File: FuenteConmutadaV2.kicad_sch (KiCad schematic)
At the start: 23 parts, among them J1 Conn_01x01_Pin, J2 Conn_01x01_Pin, J4 Conn_01x01_Pin, J5 USB_C_Receptacle_USB2.0

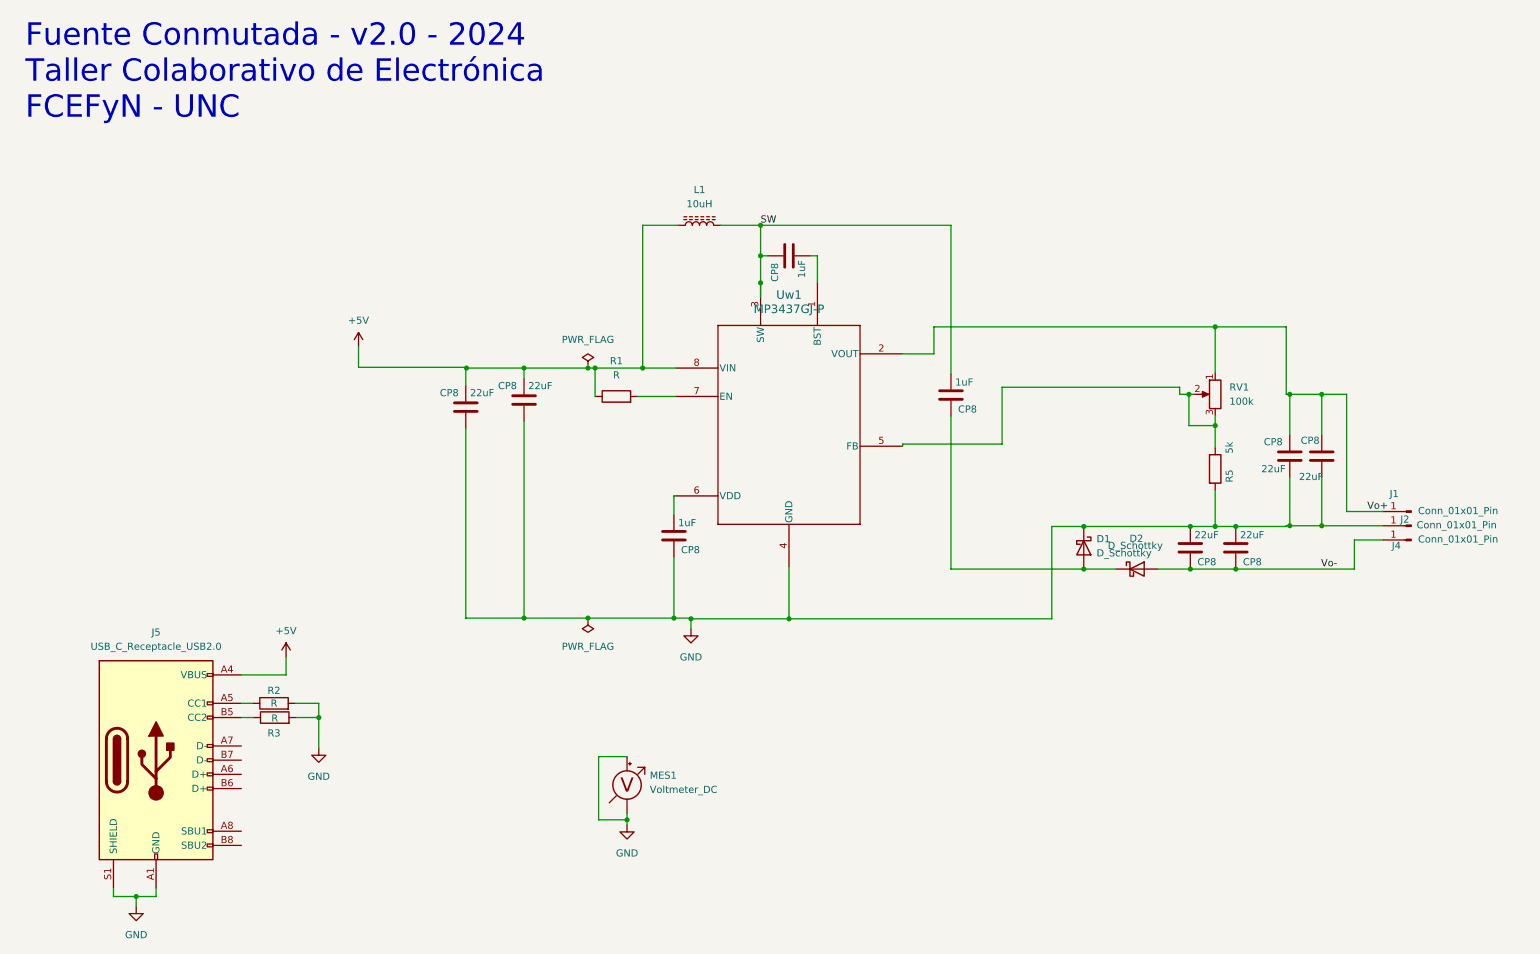
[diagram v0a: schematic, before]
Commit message: LED indicador y Resistencias de carga
Se agrego un LED rojo indicador de que se encuentra alimentada la placa, junto a resistencias con agujeros pasantes para las cargas.
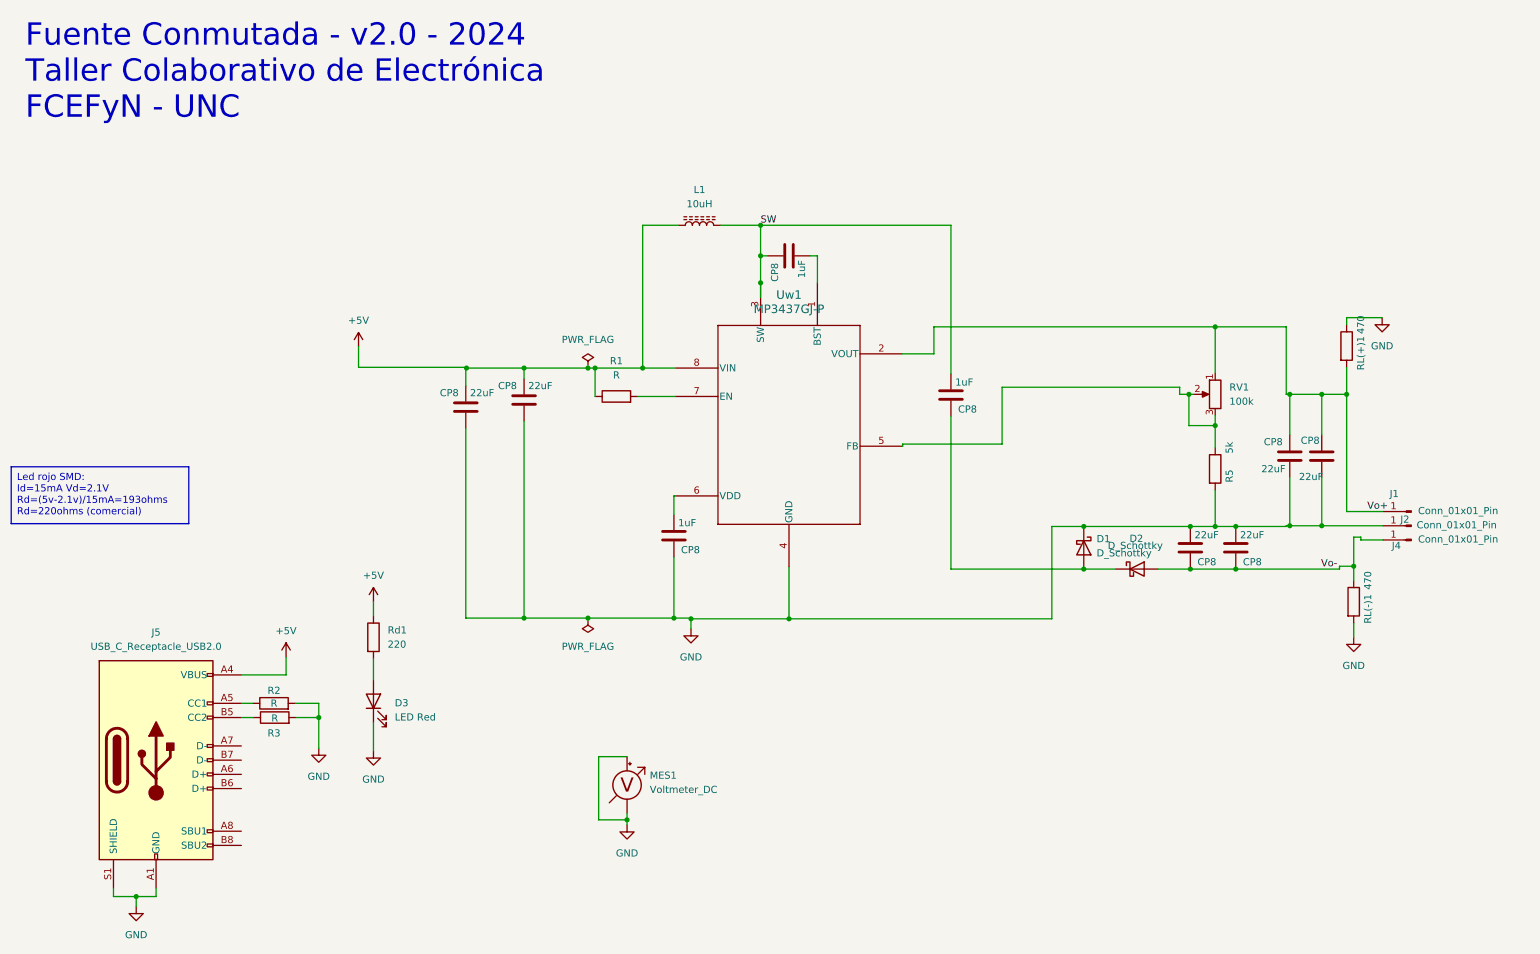
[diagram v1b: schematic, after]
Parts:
- added D3: LED Red, LED_SMD:LED_0603_1608Metric_Pad1.05x0.95mm_HandSolder, symbol Device:LED
- added RL(+)1, RL(-)1: 470, Resistor_THT:R_Axial_DIN0204_L3.6mm_D1.6mm_P5.08mm_Horizontal, symbol Device:R
- added Rd1: 220, Resistor_SMD:R_1206_3216Metric_Pad1.30x1.75mm_HandSolder, symbol Device:R
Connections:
- net +5V: now also Rd1.1
- net GND: now also D3.1 (K), RL(+)1.1, RL(-)1.2
- net Vo+: now also RL(+)1.2
- net Vo-: now also RL(-)1.1
- new net: D3.2 (A), Rd1.2

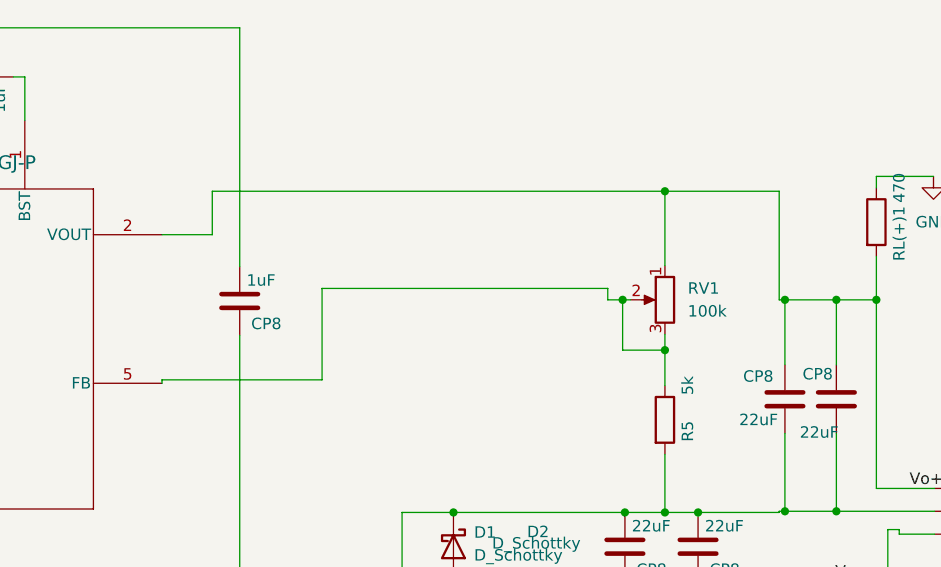
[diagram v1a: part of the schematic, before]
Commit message: Led-Huecos voltimetro y esquinas  -R paralelo
-Cambie huella de LED a 1206 y posicione junto al display.
-Agregue agujeros (3mm) para fijar el voltímetro .
- Agregue R paralelo al potenciómetro.
-cambie Huecos de las esquinas a 3mm y un margen de 5 mm (Diametro)
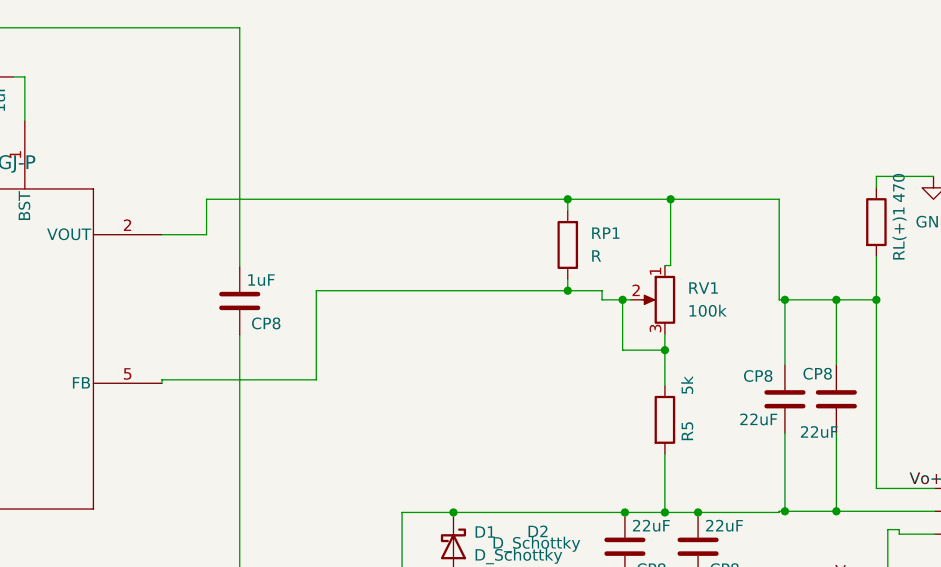
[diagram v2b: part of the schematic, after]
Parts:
- added RP1: R, Resistor_SMD:R_1206_3216Metric_Pad1.30x1.75mm_HandSolder, symbol Device:R
- D3: footprint LED_SMD:LED_0603_1608Metric_Pad1.05x0.95mm_HandSolder -> LED_SMD:LED_1206_3216Metric
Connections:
- net Vo+: now also RP1.2
- net at R5.1, RV1.2, RV1.3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: now also RP1.1
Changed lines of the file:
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@@
 	)
 	(junction
+		(at 218.44 82.55)
+		(diameter 0)
+		(color 0 0 0 0)
+	)
+	(junction
 		(at 232.918 114.808)
 		(diameter 0)
@@
 	)
 	(junction
+		(at 218.44 72.39)
+		(diameter 0)
+		(color 0 0 0 0)
+	)
+	(junction
 		(at 132.461 123.571)
 		(diameter 0)
@@
 	)
 	(junction
-		(at 229.235 71.501)
+		(at 229.87 72.39)
 		(diameter 0)
 		(color 0 0 0 0)
@@
 	(wire
 		(pts
-			(xy 241.935 71.501) (xy 241.935 83.566)
+			(xy 241.935 72.39) (xy 241.935 83.566)
 		)
 		(stroke
@@
 	(wire
 		(pts
+			(xy 218.44 82.55) (xy 222.25 82.55)
+		)
+		(stroke
+			(width 0)
+			(type default)
+		)
+	)
+	(wire
+		(pts
 			(xy 248.285 83.566) (xy 252.73 83.566)
 		)
@@
 	(wire
 		(pts
-			(xy 191.135 82.296) (xy 222.885 82.296)
+			(xy 190.5 82.55) (xy 218.44 82.55)
 		)
 		(stroke
@@
 	(wire
 		(pts
+			(xy 218.44 81.28) (xy 218.44 82.55)
+		)
+		(stroke
+			(width 0)
+			(type default)
+		)
+	)
+	(wire
+		(pts
 			(xy 153.035 114.427) (xy 153.035 123.698)
 		)
@@
 	(wire
 		(pts
-			(xy 222.885 83.566) (xy 224.536 83.566)
+			(xy 222.25 83.566) (xy 224.536 83.566)
 		)
 		(stroke
@@
 	(wire
 		(pts
+			(xy 218.44 72.39) (xy 218.44 73.66)
+		)
+		(stroke
+			(width 0)
+			(type default)
+		)
+	)
+	(wire
+		(pts
 			(xy 124.079 159.639) (xy 124.079 160.528)
 		)
@@
 	(wire
 		(pts
+			(xy 218.44 72.39) (xy 229.87 72.39)
+		)
+		(stroke
+			(width 0)
+			(type default)
+		)
+	)
+	(wire
+		(pts
 			(xy 76.073 78.74) (xy 76.073 75.057)
 		)
@@
 	(wire
 		(pts
+			(xy 229.87 79.756) (xy 229.235 79.756)
+		)
+		(stroke
+			(width 0)
+			(type default)
+		)
+	)
+	(wire
+		(pts
 			(xy 147.955 63.627) (xy 147.955 66.167)
 		)
@@
 	(wire
 		(pts
-			(xy 222.885 82.296) (xy 222.885 83.566)
+			(xy 222.25 82.55) (xy 222.25 83.566)
 		)
 		(stroke
@@
 	(wire
 		(pts
-			(xy 173.355 76.327) (xy 178.943 76.327)
+			(xy 173.355 76.327) (xy 178.308 76.327)
 		)
 		(stroke
@@
 	(wire
 		(pts
-			(xy 178.943 71.501) (xy 178.943 76.327)
+			(xy 178.308 72.39) (xy 178.308 76.327)
 		)
 		(stroke
@@
 	(wire
 		(pts
-			(xy 178.943 71.501) (xy 229.235 71.501)
+			(xy 178.308 72.39) (xy 218.44 72.39)
 		)
 		(stroke
@@
 	(wire
 		(pts
-			(xy 229.235 71.501) (xy 241.935 71.501)
+			(xy 229.87 72.39) (xy 241.935 72.39)
 		)
 		(stroke
@@
 	(wire
 		(pts
-			(xy 191.135 82.296) (xy 191.135 92.456)
+			(xy 190.5 82.55) (xy 190.5 92.456)
 		)
 		(stroke
@@
 	(wire
 		(pts
-			(xy 173.355 92.456) (xy 191.135 92.456)
+			(xy 173.355 92.456) (xy 190.5 92.456)
 		)
 		(stroke
@@
 	(wire
 		(pts
-			(xy 229.235 71.501) (xy 229.235 79.756)
+			(xy 229.87 72.39) (xy 229.87 79.756)
 		)
 		(stroke
@@
 	)
 	(symbol
+		(lib_id "Device:R")
+		(at 218.44 77.47 180)
+		(unit 1)
+		(exclude_from_sim no)
+		(in_bom yes)
+		(on_board yes)
+		(dnp no)
+		(fields_autoplaced yes)
+		(property "Reference" "RP1"
+			(at 220.98 76.1999 0)
+			(effects
+				(font
+					(size 1.27 1.27)
+				)
+				(justify right)
+			)
+		)
+		(property "Value" "R"
+			(at 220.98 78.7399 0)
+			(effects
+				(font
+					(size 1.27 1.27)
+				)
+				(justify right)
+			)
+		)
+		(property "Footprint" "Resistor_SMD:R_1206_3216Metric_Pad1.30x1.75mm_HandSolder"
+			(at 220.218 77.47 90)
+			(effects
+				(font
+					(size 1.27 1.27)
+				)
+				(hide yes)
+			)
+		)
+		(property "Datasheet" "~"
+			(at 218.44 77.47 0)
+			(effects
+				(font
+					(size 1.27 1.27)
+				)
+				(hide yes)
+			)
+		)
+		(property "Description" ""
+			(at 218.44 77.47 0)
+			(effects
+				(font
+					(size 1.27 1.27)
+				)
+				(hide yes)
+			)
+		)
+		(pin "1"
+		)
+		(pin "2"
+		)
+		(instances
+			(project "FuenteConmutadaV2"
+				(path "/d69a48d3-cc9a-476a-8449-ca4ce55f09c5"
+					(reference "RP1")
+					(unit 1)
+				)
+			)
+		)
+	)
+	(symbol
 		(lib_id "power:GND")
 		(at 124.079 160.528 0)
@@
 			)
 		)
-		(property "Footprint" "LED_SMD:LED_0603_1608Metric_Pad1.05x0.95mm_HandSolder"
+		(property "Footprint" "LED_SMD:LED_1206_3216Metric"
 			(at 78.74 138.43 0)
 			(effects
